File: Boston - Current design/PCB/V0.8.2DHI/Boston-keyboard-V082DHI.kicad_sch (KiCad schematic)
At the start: 320 parts, among them J701 Conn_01x04_MountingPin, J702 Conn_01x03, J705 Conn_01x04_MountingPin, J706 Conn_ARM_JTAG_SWD_10, Q701 DTC123J, SW1 MXSwitch, SW10 MXSwitch, SW100 MXSwitch, SW101 MXSwitch, SW102 MXSwitch, SW103 MXSwitch, SW104 MXSwitch, SW105-1 MXSwitch, SW105-2 MXSwitch, SW106 MXSwitch, SW107 MXSwitch, SW108 MXSwitch, SW109 MXSwitch, SW11 MXSwitch, SW110 MXSwitch, SW111 MXSwitch, SW112 MXSwitch, SW113 MXSwitch, SW114 MXSwitch, SW115 MXSwitch, SW116 MXSwitch, SW117 MXSwitch, SW118 MXSwitch, SW119 MXSwitch, SW12 MXSwitch, SW120 MXSwitch, SW121 MXSwitch, SW122 MXSwitch, SW123 MXSwitch, SW124-1 MXSwitch, SW124-2 MXSwitch, SW125 MXSwitch, SW126 Rotary_Encoder_Switch_Chassis, SW127 MXSwitch, SW128 MXSwitch, SW129 MXSwitch, SW13 MXSwitch, SW14 MXSwitch, SW15 MXSwitch, SW16 MXSwitch, SW17 MXSwitch, SW18 MXSwitch, SW19 MXSwitch, SW2 MXSwitch, SW20 MXSwitch, SW200 SW_Push, SW21 MXSwitch, SW22 MXSwitch, SW23 MXSwitch, SW24 MXSwitch, SW25 MXSwitch, SW26 MXSwitch, SW27 MXSwitch, SW28 MXSwitch, SW29 MXSwitch, SW3 MXSwitch, SW30 MXSwitch, SW31 MXSwitch, SW32 MXSwitch, SW33 MXSwitch, SW34 MXSwitch, SW35 MXSwitch, SW36 MXSwitch, SW37 MXSwitch, SW38 MXSwitch, SW39-1 MXSwitch, SW39-2 MXSwitch, SW4 MXSwitch, SW40 MXSwitch, SW41 MXSwitch, SW42 MXSwitch, SW43 MXSwitch, SW44 MXSwitch, SW45 MXSwitch, SW46 MXSwitch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

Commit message: Took initial pass at designing the V0.8.2DHI
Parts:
- added D12, D83: 1N4148, acheronComponents:D_SOD-123, symbol Diode:1N4148
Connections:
- net Row5: now also D83.1 (K); no longer SW83.2 (Row)
- net Row6: now also D12.1 (K); no longer SW12.2 (Row)
- new net: D83.2 (A), SW83.2 (Row)
- new net: D12.2 (A), SW12.2 (Row)
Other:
- moved on the sheet: D5
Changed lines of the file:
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@@
 (kicad_sch (version 20230121) (generator eeschema)
   (paper "D")
-  (junction (at 34.29 204.47) (diameter 0.3048) (color 0 0 0 0)
-  )
   (junction (at 148.59 35.56) (diameter 0.3048) (color 0 0 0 0)
   )
@@
   (junction (at 571.5 176.53) (diameter 0.3048) (color 0 0 0 0)
   )
-  (junction (at 457.2 157.48) (diameter 0.3048) (color 0 0 0 0)
-  )
   (junction (at 388.62 157.48) (diameter 0.3048) (color 0 0 0 0)
   )
@@
   (junction (at 553.72 53.34) (diameter 0.3048) (color 0 0 0 0)
   )
-  (junction (at 45.72 185.42) (diameter 0.3048) (color 0 0 0 0)
-  )
   (junction (at 34.29 120.65) (diameter 0.3048) (color 0 0 0 0)
   )
@@
   (junction (at 629.92 176.53) (diameter 0.3048) (color 0 0 0 0)
   )
-  (junction (at 80.01 185.42) (diameter 0.3048) (color 0 0 0 0)
-  )
   (junction (at 448.31 493.395) (diameter 0.3048) (color 0 0 0 0)
   )
@@
   (junction (at 308.61 176.53) (diameter 0.3048) (color 0 0 0 0)
   )
+  (junction (at 80.01 185.42) (diameter 0) (color 0 0 0 0)
+  )
   (junction (at 171.45 53.34) (diameter 0.3048) (color 0 0 0 0)
   )
@@
   (junction (at 476.25 459.74) (diameter 0.3048) (color 0 0 0 0)
   )
+  (junction (at 34.29 205.74) (diameter 0) (color 0 0 0 0)
+  )
   (junction (at 462.28 219.71) (diameter 0.3048) (color 0 0 0 0)
   )
@@
   (junction (at 411.48 81.28) (diameter 0.3048) (color 0 0 0 0)
   )
+  (junction (at 457.2 157.48) (diameter 0) (color 0 0 0 0)
+  )
   (junction (at 388.62 62.23) (diameter 0.3048) (color 0 0 0 0)
   )
@@
   (junction (at 457.2 62.23) (diameter 0.3048) (color 0 0 0 0)
   )
+  (junction (at 46.99 185.42) (diameter 0) (color 0 0 0 0)
+  )
   (junction (at 172.72 459.105) (diameter 0.3048) (color 0 0 0 0)
   )
@@
     (stroke (width 0) (type solid))
   )
+  (wire (pts (xy 46.99 185.42) (xy 80.01 185.42))
+    (stroke (width 0) (type solid))
+  )
   (wire (pts (xy 473.71 459.74) (xy 473.71 461.01))
     (stroke (width 0) (type solid))
@@
     (stroke (width 0) (type solid))
   )
-  (wire (pts (xy 422.91 157.48) (xy 457.2 157.48))
-    (stroke (width 0) (type solid))
-  )
   (wire (pts (xy 600.71 204.47) (xy 600.71 176.53))
     (stroke (width 0) (type solid))
@@
     (stroke (width 0.9906) (type dash))
   )
-  (wire (pts (xy 80.01 185.42) (xy 80.01 195.58))
-    (stroke (width 0) (type default))
-  )
   (wire (pts (xy 388.62 35.56) (xy 354.33 35.56))
     (stroke (width 0) (type solid))
@@
     (stroke (width 0) (type solid))
   )
-  (wire (pts (xy 35.56 204.47) (xy 34.29 204.47))
-    (stroke (width 0) (type solid))
-  )
   (wire (pts (xy 448.31 336.55) (xy 454.66 336.55))
     (stroke (width 0) (type solid))
@@
     (stroke (width 0) (type solid))
   )
+  (wire (pts (xy 457.2 157.48) (xy 491.49 157.48))
+    (stroke (width 0) (type solid))
+  )
   (wire (pts (xy 641.35 185.42) (xy 612.14 185.42))
     (stroke (width 0) (type solid))
@@
     (stroke (width 0) (type solid))
   )
+  (wire (pts (xy 457.2 157.48) (xy 457.2 160.02))
+    (stroke (width 0) (type default))
+  )
   (wire (pts (xy 720.09 30.48) (xy 721.36 30.48))
     (stroke (width 0) (type default))
@@
     (stroke (width 0) (type solid))
   )
-  (wire (pts (xy 45.72 185.42) (xy 45.72 187.96))
-    (stroke (width 0) (type solid))
-  )
   (wire (pts (xy 819.785 485.14) (xy 819.785 489.585))
     (stroke (width 0) (type solid))
@@
     (stroke (width 0) (type solid))
   )
-  (wire (pts (xy 46.99 195.58) (xy 45.72 195.58))
-    (stroke (width 0) (type solid))
-  )
   (wire (pts (xy 740.41 152.4) (xy 750.57 152.4))
     (stroke (width 0) (type default))
@@
     (stroke (width 0) (type solid))
   )
-  (wire (pts (xy 46.99 196.85) (xy 46.99 195.58))
-    (stroke (width 0) (type solid))
-  )
   (wire (pts (xy 148.59 36.83) (xy 148.59 35.56))
     (stroke (width 0) (type solid))
@@
     (stroke (width 0) (type solid))
   )
+  (wire (pts (xy 46.99 193.04) (xy 46.99 196.85))
+    (stroke (width 0) (type default))
+  )
   (wire (pts (xy 426.72 493.395) (xy 448.31 493.395))
     (stroke (width 0) (type solid))
@@
     (stroke (width 0) (type solid))
   )
-  (wire (pts (xy 35.56 205.74) (xy 35.56 204.47))
-    (stroke (width 0) (type solid))
-  )
   (wire (pts (xy 285.75 36.83) (xy 285.75 35.56))
     (stroke (width 0) (type solid))
@@
     (stroke (width 0) (type solid))
   )
+  (wire (pts (xy 80.01 185.42) (xy 114.3 185.42))
+    (stroke (width 0) (type solid))
+  )
   (wire (pts (xy 137.16 176.53) (xy 137.16 148.59))
     (stroke (width 0) (type solid))
@@
     (stroke (width 0) (type solid))
   )
+  (wire (pts (xy 34.29 205.74) (xy 38.1 205.74))
+    (stroke (width 0) (type default))
+  )
   (wire (pts (xy 208.28 176.53) (xy 205.74 176.53))
     (stroke (width 0) (type solid))
@@
     (stroke (width 0) (type solid))
   )
+  (wire (pts (xy 80.01 193.04) (xy 80.01 195.58))
+    (stroke (width 0) (type default))
+  )
   (wire (pts (xy 320.04 129.54) (xy 354.33 129.54))
     (stroke (width 0) (type solid))
@@
     (stroke (width 0) (type default))
   )
-  (wire (pts (xy 38.1 205.74) (xy 35.56 205.74))
-    (stroke (width 0) (type solid))
-  )
-  (wire (pts (xy 34.29 176.53) (xy 34.29 204.47))
-    (stroke (width 0) (type solid))
-  )
   (polyline (pts (xy 71.755 501.65) (xy 15.24 501.65))
     (stroke (width 0.9906) (type dash))
@@
     (stroke (width 0) (type solid))
   )
+  (wire (pts (xy 34.29 205.74) (xy 34.29 233.68))
+    (stroke (width 0) (type solid))
+  )
   (wire (pts (xy 182.88 62.23) (xy 217.17 62.23))
     (stroke (width 0) (type solid))
@@
     (stroke (width 0) (type solid))
   )
-  (wire (pts (xy 25.4 185.42) (xy 45.72 185.42))
-    (stroke (width 0) (type solid))
-  )
   (wire (pts (xy 603.25 204.47) (xy 600.71 204.47))
     (stroke (width 0) (type solid))
@@
     (stroke (width 0) (type solid))
   )
-  (wire (pts (xy 457.2 157.48) (xy 491.49 157.48))
+  (wire (pts (xy 422.91 157.48) (xy 457.2 157.48))
     (stroke (width 0) (type solid))
   )
@@
     (stroke (width 0) (type solid))
   )
-  (wire (pts (xy 457.2 157.48) (xy 457.2 167.64))
-    (stroke (width 0) (type default))
-  )
   (wire (pts (xy 379.73 120.65) (xy 377.19 120.65))
     (stroke (width 0) (type solid))
@@
     (stroke (width 0) (type solid))
   )
-  (wire (pts (xy 45.72 185.42) (xy 80.01 185.42))
+  (wire (pts (xy 25.4 185.42) (xy 46.99 185.42))
     (stroke (width 0) (type solid))
   )
@@
     (stroke (width 0) (type solid))
   )
-  (wire (pts (xy 80.01 185.42) (xy 114.3 185.42))
-    (stroke (width 0) (type solid))
-  )
-  (wire (pts (xy 34.29 204.47) (xy 34.29 233.68))
+  (wire (pts (xy 34.29 176.53) (xy 34.29 205.74))
     (stroke (width 0) (type solid))
   )
@@
     (effects (font (size 1.27 1.27)) (justify left bottom))
   )
-  (text "ISO Enter\n" (at 510.54 177.8 0)
+  (text "ISO Enter\n" (at 487.68 179.07 0)
     (effects (font (size 1.27 1.27)) (justify left bottom))
   )
@@
     )
   )
-  (symbol (lib_id "Diode:1N4148") (at 45.72 191.77 270) (unit 1)
+  (symbol (lib_id "Diode:1N4148") (at 46.99 189.23 270) (unit 1)
     (in_bom yes) (on_board yes) (dnp no)
-    (property "Reference" "D5" (at 47.7266 190.6016 90)
+    (property "Reference" "D5" (at 48.9966 188.0616 90)
       (effects (font (size 1.27 1.27)) (justify left))
     )
-    (property "Value" "1N4148" (at 47.7266 192.913 90)
+    (property "Value" "1N4148" (at 48.9966 190.373 90)
       (effects (font (size 1.27 1.27)) (justify left))
     )
-    (property "Footprint" "acheronComponents:D_SOD-123" (at 41.275 191.77 0)
+    (property "Footprint" "acheronComponents:D_SOD-123" (at 42.545 189.23 0)
       (effects (font (size 1.27 1.27)) hide)
     )
-    (property "Datasheet" "https://assets.nexperia.com/documents/data-sheet/1N4148_1N4448.pdf" (at 45.72 191.77 0)
+    (property "Datasheet" "https://assets.nexperia.com/documents/data-sheet/1N4148_1N4448.pdf" (at 46.99 189.23 0)
       (effects (font (size 1.27 1.27)) hide)
     )
@@
     )
   )
+  (symbol (lib_id "Diode:1N4148") (at 80.01 189.23 270) (unit 1)
+    (in_bom yes) (on_board yes) (dnp no)
+    (property "Reference" "D12" (at 82.0166 188.0616 90)
+      (effects (font (size 1.27 1.27)) (justify left))
+    )
+    (property "Value" "1N4148" (at 82.0166 190.373 90)
+      (effects (font (size 1.27 1.27)) (justify left))
+    )
+    (property "Footprint" "acheronComponents:D_SOD-123" (at 75.565 189.23 0)
+      (effects (font (size 1.27 1.27)) hide)
+    )
+    (property "Datasheet" "https://assets.nexperia.com/documents/data-sheet/1N4148_1N4448.pdf" (at 80.01 189.23 0)
+      (effects (font (size 1.27 1.27)) hide)
+    )
+    (pin "1")
+    (pin "2")
+    (instances
+      (project "Boston-keyboard-V082DHI"
+        (path "/e63e39d7-6ac0-4ffd-8aa3-1841a4541b55"
+          (reference "D12") (unit 1)
+        )
+      )
+    )
+  )
   (symbol (lib_id "Boston-keyboard-rescue:MXSwitch-Acheron") (at 80.01 204.47 0) (unit 1)
     (in_bom yes) (on_board yes) (dnp no)
@@
         )
       )
+    )
+  )
+  (symbol (lib_id "Diode:1N4148") (at 457.2 163.83 270) (unit 1)
+    (in_bom yes) (on_board yes) (dnp no)
+    (property "Reference" "D83" (at 459.2066 162.6616 90)
+      (effects (font (size 1.27 1.27)) (justify left))
+    )
+    (property "Value" "1N4148" (at 459.2066 164.973 90)
+      (effects (font (size 1.27 1.27)) (justify left))
+    )
+    (property "Footprint" "acheronComponents:D_SOD-123" (at 452.755 163.83 0)
+      (effects (font (size 1.27 1.27)) hide)
+    )
+    (property "Datasheet" "https://assets.nexperia.com/documents/data-sheet/1N4148_1N4448.pdf" (at 457.2 163.83 0)
+      (effects (font (size 1.27 1.27)) hide)
+    )
+    (pin "1")
+    (pin "2")
+    (instances
+      (project "Boston-keyboard-V082DHI"
+        (path "/e63e39d7-6ac0-4ffd-8aa3-1841a4541b55"
+          (reference "D83") (unit 1)
+        )
+      )

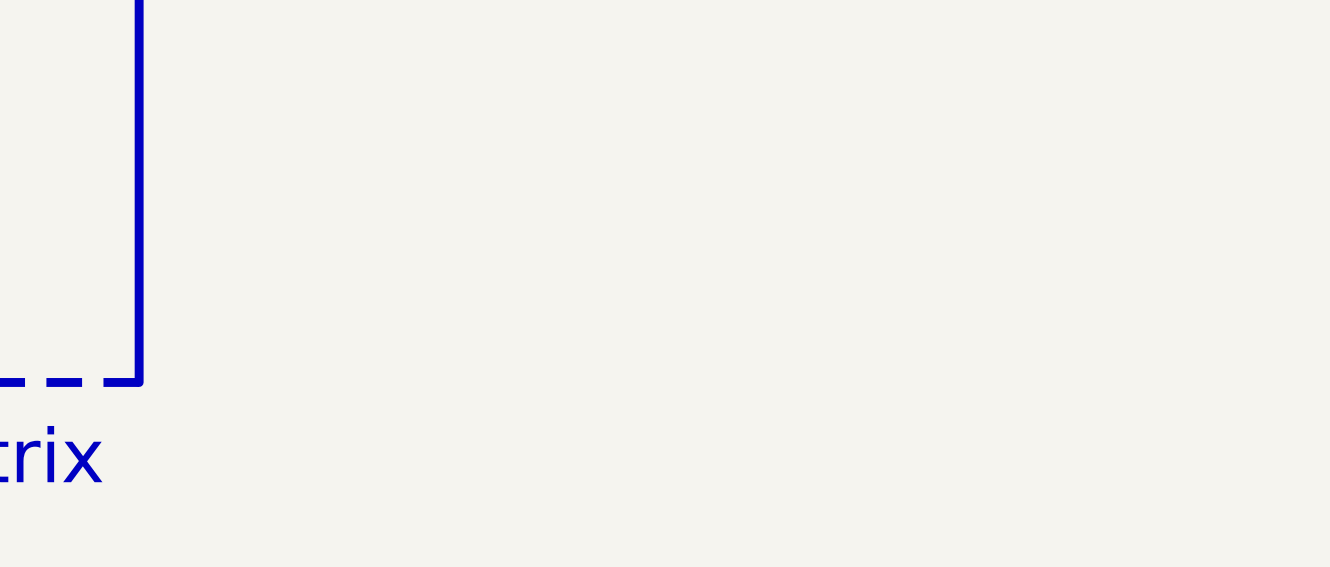
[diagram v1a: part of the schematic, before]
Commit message: Added note that SW123 and SW124-2 were accidentally swapped in the PCB layout
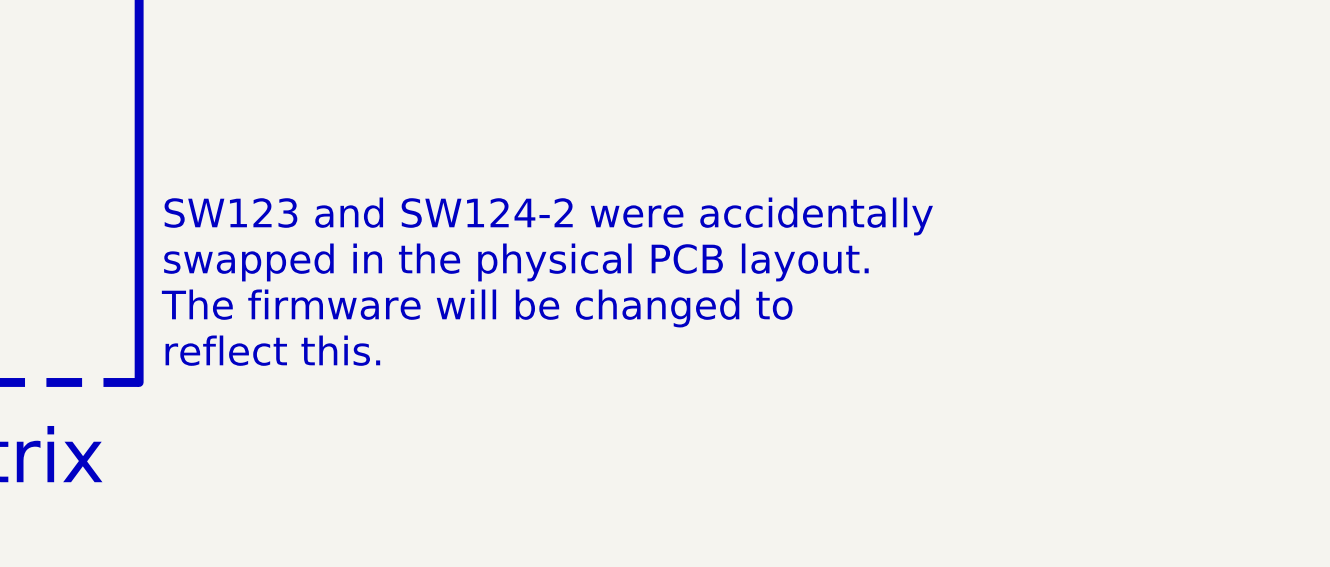
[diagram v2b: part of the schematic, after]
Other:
- note added: "SW123 and SW124-2 were accidentally swapped in the physical PCB layout. The firmware will be changed to reflect this."
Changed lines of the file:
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@@
     (effects (font (size 1.27 1.27)) (justify left bottom))
+  )
+  (text "SW123 and SW124-2 were accidentally \nswapped in the physical PCB layout. \nThe firmware will be changed to \nreflect this."
+    (at 693.42 252.73 0)
+    (effects (font (size 3.175 3.175)) (justify left bottom))
   )
   (text "[{" (at 421.64 153.67 0)
